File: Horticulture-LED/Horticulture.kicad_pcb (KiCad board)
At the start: 2 copper layers, 220 x 22 mm, 59 parts, among them J3 Conn_01x04_Male, J4 Conn_01x04_Male, U1 TLE4309, U2 TLE4309, U3 TLE4309, U4 TLE4309, U5 PCA9633DP2

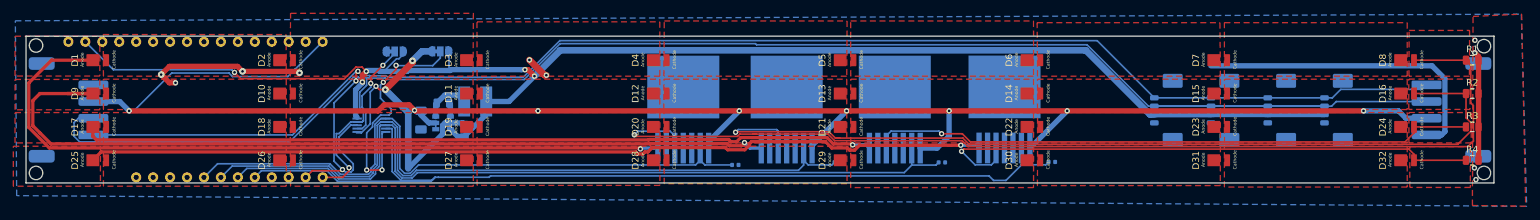
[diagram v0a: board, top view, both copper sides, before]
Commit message: fixes #10 #11 #12
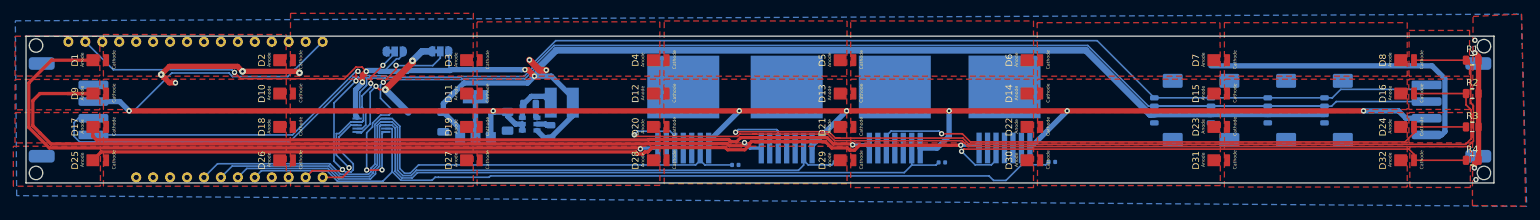
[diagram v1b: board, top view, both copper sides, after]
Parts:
- added Cldo1: 4.7uF, 50V, Capacitor_SMD:C_1206_3216Metric, B.Cu at (102.5, 92.9)
- added U6: MCP1703A-1502_SOT223, Package_TO_SOT_SMD:SOT-223-3_TabPin2, B.Cu at (107.4, 92.2)
- Cboot1: value 100nF -> 100nF, X7R/X5R, 16V
- Cin1: value 4.7uF -> 4.7uF, 50V
- Cout1: value 22uF -> 22uF, X7R/X5R, 10V
- D1, D2, D25, D26, D27, D28, D29, D3, D30, D31, D32, D4, D5, D6, D7, D8: value LED -> LED, Purple (2.5% Blue), L1SP-PRP0002800000
- D10, D11, D12, D13, D14, D15, D16, D9: value LED -> LED, Royal Blue, L1SP-RYL0002800000
- D17, D18, D19, D20, D21, D22, D23, D24: value LED -> LED, Lime, L1SP-LME0002800000
- moved Cboot1 13.0 mm to (115.5, 90.2)
- moved Cin1 13.0 mm to (112.2, 92.8)
- moved Cout1 13.0 mm to (118.6, 94.3)
- moved L1 13.0 mm to (120.3, 90.0)
- moved VR1 13.0 mm to (115.5, 93.2)
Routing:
- net +3.3V: track 239.9 -> 261.0 mm
- net GND: track 133.1 -> 122.5 mm
- net UC-pwm4: track 138.9 -> 132.9 mm
- net +24vdc: track 275.4 -> 279.3 mm, vias 8 -> 7
- net Net-(D16-Pad1): track 135.1 -> 135.8 mm
